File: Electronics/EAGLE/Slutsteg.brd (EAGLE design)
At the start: 100 x 160 mm, 151 parts, among them CN1 OSTYK33102030-2, CN2 OSTYK33102030-2, CN3 OSTYK33102030-2, CN4 OSTYK33102030-2, IC1 SPX1117M3-L-3-3_TR, IC10 LM324D, IC11 L78M12ABDT-TR, IC3 ESP32-WROVER-IE-4MB, IC4 TM8211, IC5 LM358LVIDR, IC6 TPA3244DDWR, IC7 TPA3251D2DDVR, IC8 LM324D, IC9 LM324D, J1 0532610671, SW1 PDB181-K420F-103A2, SW2 PDB181-K420F-103A2

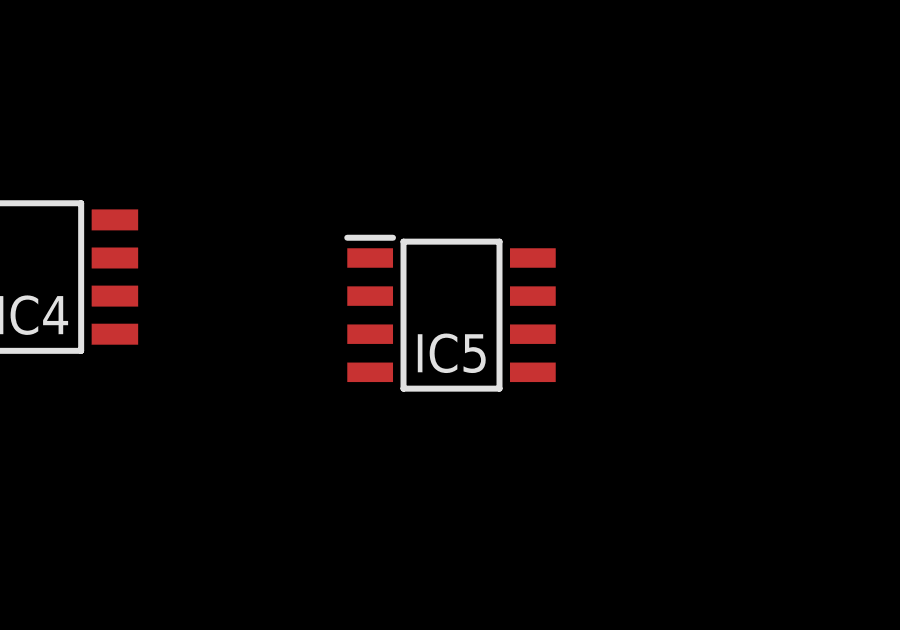
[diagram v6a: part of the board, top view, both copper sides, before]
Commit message: Changed OP-AMP for the DAC
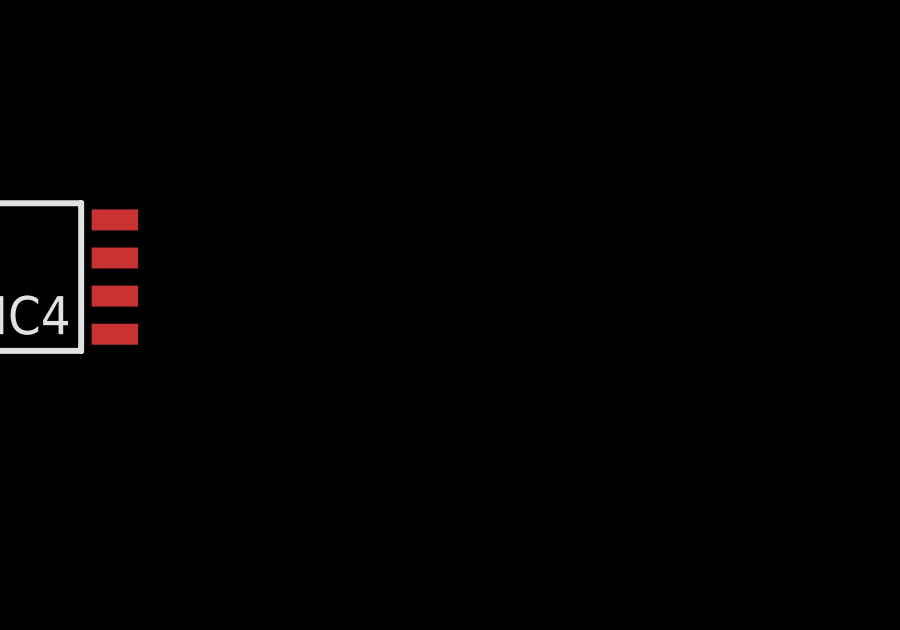
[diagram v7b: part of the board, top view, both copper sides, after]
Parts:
- removed IC5: LM358LVIDR, SamacSys_Parts:SOIC127P600X175-8N
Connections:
- net BLE-L: now also IC10.6, IC10.7; no longer IC5.6, IC5.7
- net BLE-R: now also IC10.1, IC10.2; no longer IC5.1, IC5.2
- net GND: now also IC10.11; no longer IC5.4
- net N$79: now also IC10.3; no longer IC5.3
- net N$81: now also IC10.5; no longer IC5.5
- net VDD: now also IC10.4; no longer IC5.8
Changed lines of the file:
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@@
 <attribute name="VALUE" x="-205.56" y="146.59" size="1.27" layer="27"/>
-</element>
-<element name="IC5" library="SamacSys_Parts" package="SOIC127P600X175-8N" override_package3d_urn="urn:adsk.eagle:package:27158186/2" override_package_urn="urn:adsk.eagle:footprint:27158187/1" override_locally_modified="yes" value="LM358LVIDR" x="-182.7" y="192.31" smashed="yes">
-<attribute name="ARROW_PART_NUMBER" value="LM358LVIDR" x="-182.7" y="192.31" size="1.778" layer="27" display="off"/>
-<attribute name="ARROW_PRICE-STOCK" value="https://www.arrow.com/en/products/lm358lvidr/texas-instruments" x="-182.7" y="192.31" size="1.778" layer="27" display="off"/>
-<attribute name="DESCRIPTION" value="2-Channel Industry-Standard Low-Voltage Operational Amplifier" x="-182.7" y="192.31" size="1.778" layer="27" display="off"/>
-<attribute name="HEIGHT" value="1.75mm" x="-182.7" y="192.31" size="1.778" layer="27" display="off"/>
-<attribute name="MANUFACTURER_NAME" value="Texas Instruments" x="-182.7" y="192.31" size="1.778" layer="27" display="off"/>
-<attribute name="MANUFACTURER_PART_NUMBER" value="LM358LVIDR" x="-182.7" y="192.31" size="1.778" layer="27" display="off"/>
-<attribute name="MOUSER_PART_NUMBER" value="595-LM358LVIDR" x="-182.7" y="192.31" size="1.778" layer="27" display="off"/>
-<attribute name="MOUSER_PRICE-STOCK" value="https://www.mouser.co.uk/ProductDetail/Texas-Instruments/LM358LVIDR/?qs=qSfuJ%252Bfl%2Fd53U%2FPkf9lZVw%3D%3D" x="-182.7" y="192.31" size="1.778" layer="27" display="off"/>
-<attribute name="NAME" x="-182.7" y="191.04" size="1.27" layer="25" align="center"/>
-<attribute name="VALUE" x="-182.7" y="194.85" size="1.27" layer="27" align="center"/>
 </element>
 <element name="R6" library="rcl" library_urn="urn:adsk.eagle:library:334" package="R0603" package3d_urn="urn:adsk.eagle:package:23555/3" value="10k/5%/0.1W" x="-206.83" y="136.43" smashed="yes">
@@
 <contactref element="C8" pad="2"/>
 <contactref element="C11" pad="2"/>
-<contactref element="IC5" pad="4"/>
 <contactref element="C13" pad="2"/>
 <contactref element="R7" pad="2"/>
-<contactref element="R10" pad="2"/>
 <contactref element="IC11" pad="4"/>
 <contactref element="C5" pad="2"/>
@@
 <contactref element="IC1" pad="1"/>
 <contactref element="C6" pad="2"/>
+<contactref element="R10" pad="2"/>
+<contactref element="IC10" pad="11"/>
 <wire x1="116.12" y1="129.87" x2="114.42" y2="134.95" width="0" layer="19" extent="1-1"/>
 <wire x1="114.42" y1="145.11" x2="114.42" y2="134.95" width="0" layer="19" extent="1-1"/>
@@
 <wire x1="-155.76" y1="225.86" x2="-157.46" y2="229.67" width="0" layer="19" extent="1-1"/>
 <wire x1="-161.518" y1="206.81" x2="-155.76" y2="225.86" width="0" layer="19" extent="1-1"/>
-<wire x1="-185.412" y1="190.405" x2="-161.518" y2="206.81" width="0" layer="19" extent="1-1"/>
-<wire x1="-199.42" y1="191.675" x2="-185.412" y2="190.405" width="0" layer="19" extent="1-1"/>
+<wire x1="-193.545" y1="237.764" x2="-157.46" y2="229.67" width="0" layer="19" extent="1-1"/>
+<wire x1="-199.42" y1="191.675" x2="-161.518" y2="206.81" width="0" layer="19" extent="1-1"/>
 <wire x1="-203.34" y1="189.77" x2="-199.42" y2="191.675" width="0" layer="19" extent="1-1"/>
 <wire x1="-203.34" y1="177.07" x2="-203.34" y2="189.77" width="0" layer="19" extent="1-1"/>
@@
 <wire x1="-205.98" y1="80.55" x2="-205.98" y2="105.95" width="0" layer="19" extent="1-1"/>
 <wire x1="-205.98" y1="75.47" x2="-205.98" y2="80.55" width="0" layer="19" extent="1-1"/>
-<wire x1="-193.545" y1="237.764" x2="-157.46" y2="229.67" width="0" layer="19" extent="1-1"/>
 <wire x1="-164.65" y1="124.26" x2="-205.98" y2="116.11" width="0" layer="19" extent="1-1"/>
 <wire x1="-164.65" y1="129.34" x2="-164.65" y2="124.26" width="0" layer="19" extent="1-1"/>
-<wire x1="-199.55" y1="-15" x2="-205.98" y2="75.47" width="0" layer="19" extent="1-1"/>
+<wire x1="-201.288" y1="-6" x2="-205.98" y2="75.47" width="0" layer="19" extent="1-1"/>
+<wire x1="-199.55" y1="-15" x2="-201.288" y2="-6" width="0" layer="19" extent="1-1"/>
 <wire x1="-208" y1="-20.7" x2="-199.55" y2="-15" width="0" layer="19" extent="1-1"/>
 <wire x1="-211.05" y1="-30" x2="-208" y2="-20.7" width="0" layer="19" extent="1-1"/>
@@
 <contactref element="C77" pad="1"/>
 <contactref element="C74" pad="1"/>
-<contactref element="IC5" pad="8"/>
 <contactref element="IC11" pad="3"/>
 <contactref element="D1" pad="1"/>
 <contactref element="IC1" pad="3"/>
 <contactref element="C4" pad="1"/>
+<contactref element="IC10" pad="4"/>
 <wire x1="-208" y1="-25.3" x2="-212.95" y2="-30" width="0" layer="19" extent="1-1"/>
 <wire x1="-206.35" y1="-17.28" x2="-208" y2="-25.3" width="0" layer="19" extent="1-1"/>
-<wire x1="-166.35" y1="124.26" x2="-206.35" y2="-17.28" width="0" layer="19" extent="1-1"/>
+<wire x1="-206.712" y1="-6" x2="-206.35" y2="-17.28" width="0" layer="19" extent="1-1"/>
+<wire x1="-166.35" y1="124.26" x2="-206.712" y2="-6" width="0" layer="19" extent="1-1"/>
 <wire x1="-166.35" y1="129.34" x2="-166.35" y2="124.26" width="0" layer="19" extent="1-1"/>
-<wire x1="-179.988" y1="194.215" x2="-166.35" y2="129.34" width="0" layer="19" extent="1-1"/>
-<wire x1="-166.942" y1="206.81" x2="-179.988" y2="194.215" width="0" layer="19" extent="1-1"/>
-<wire x1="-203.35" y1="199.93" x2="-179.988" y2="194.215" width="0" layer="19" extent="1-1"/>
+<wire x1="-166.942" y1="206.81" x2="-166.35" y2="129.34" width="0" layer="19" extent="1-1"/>
 <wire x1="-155.76" y1="233.48" x2="-166.942" y2="206.81" width="0" layer="19" extent="1-1"/>
 <wire x1="-155.76" y1="244.91" x2="-155.76" y2="233.48" width="0" layer="19" extent="1-1"/>
 <wire x1="-158.052" y1="261.42" x2="-155.76" y2="244.91" width="0" layer="19" extent="1-1"/>
 <wire x1="-137.98" y1="291.9" x2="-158.052" y2="261.42" width="0" layer="19" extent="1-1"/>
+<wire x1="-203.35" y1="199.93" x2="-166.942" y2="206.81" width="0" layer="19" extent="1-1"/>
 <wire x1="-16.55" y1="215.27" x2="-155.76" y2="233.48" width="0" layer="19" extent="1-1"/>
 <wire x1="-16.55" y1="210.19" x2="-16.55" y2="215.27" width="0" layer="19" extent="1-1"/>
@@
 </signal>
 <signal name="BLE-R">
-<contactref element="IC5" pad="1"/>
-<contactref element="IC5" pad="2"/>
 <contactref element="C9" pad="1"/>
-<wire x1="-185.412" y1="192.945" x2="-207.68" y2="126.27" width="0" layer="19" extent="1-1"/>
-<wire x1="-185.412" y1="194.215" x2="-185.412" y2="192.945" width="0" layer="19" extent="1-1"/>
-</signal>
-<signal name="BLE-L">
-<contactref element="IC5" pad="7"/>
-<contactref element="C14" pad="1"/>
-<contactref element="IC5" pad="6"/>
-<wire x1="-179.988" y1="191.675" x2="-207.68" y2="90.71" width="0" layer="19" extent="1-1"/>
-<wire x1="-179.988" y1="192.945" x2="-179.988" y2="191.675" width="0" layer="19" extent="1-1"/>
+<contactref element="IC10" pad="1"/>
+<contactref element="IC10" pad="2"/>
+<wire x1="-206.712" y1="-2.19" x2="-206.712" y2="-3.46" width="0" layer="19" extent="1-1"/>
+<wire x1="-207.68" y1="126.27" x2="-206.712" y2="-2.19" width="0" layer="19" extent="1-1"/>
 </signal>
 <signal name="N$46">
@@
 <signal name="N$79">
 <contactref element="R8" pad="1"/>
-<contactref element="IC5" pad="3"/>
 <contactref element="C10" pad="1"/>
+<contactref element="IC10" pad="3"/>
+<wire x1="-207.68" y1="121.19" x2="-206.712" y2="-4.73" width="0" layer="19" extent="1-1"/>
 <wire x1="-207.68" y1="131.35" x2="-207.68" y2="121.19" width="0" layer="19" extent="1-1"/>
-<wire x1="-185.412" y1="191.675" x2="-207.68" y2="131.35" width="0" layer="19" extent="1-1"/>
 </signal>
 <signal name="N$80">
@@
 </signal>
 <signal name="N$81">
-<contactref element="IC5" pad="5"/>
+<contactref element="R9" pad="2"/>
+<contactref element="IC10" pad="5"/>
 <contactref element="C12" pad="1"/>
-<contactref element="R9" pad="2"/>
+<wire x1="-205.98" y1="100.87" x2="-206.712" y2="-7.27" width="0" layer="19" extent="1-1"/>
 <wire x1="-207.68" y1="111.03" x2="-205.98" y2="100.87" width="0" layer="19" extent="1-1"/>
-<wire x1="-179.988" y1="190.405" x2="-207.68" y2="111.03" width="0" layer="19" extent="1-1"/>
 </signal>
 <signal name="N$82">
@@
 </signal>
 <signal name="N$83">
-<contactref element="C14" pad="2"/>
 <contactref element="R9" pad="1"/>
 <contactref element="R11" pad="2"/>
+<contactref element="C14" pad="2"/>
 <contactref element="R10" pad="1"/>
 <wire x1="-205.98" y1="90.71" x2="-207.68" y2="75.47" width="0" layer="19" extent="1-1"/>
@@
 <contactref element="C22" pad="1"/>
 </signal>
+<signal name="BLE-L">
+<contactref element="IC10" pad="7"/>
+<contactref element="IC10" pad="6"/>
+<contactref element="C14" pad="1"/>
+<wire x1="-206.712" y1="-8.54" x2="-206.712" y2="-9.81" width="0" layer="19" extent="1-1"/>
+<wire x1="-207.68" y1="90.71" x2="-206.712" y2="-8.54" width="0" layer="19" extent="1-1"/>
+</signal>
 </signals>

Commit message: Changed footprints for caps
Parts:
- removed C76: 1uF/25V, rcl:C0603
- added C25: 1uF/50V, rcl:C0805
- C78, C79: value 1uF/25V -> 1uF/50V; device rcl:C0603 -> rcl:C0805
- moved C79 334.9 mm to (-212.0, -93.0)
- moved C78 331.8 mm to (-212.0, -86.0)
- moved J1 303.9 mm to (95.2, 152.3), turned to 90 degrees
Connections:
- net GND: now also C79.2; no longer C76.2
- net N$46: now also C25.1; no longer C78.2
- net N$47: now also C78.1; no longer C79.2
- net N$50: now also C79.1; no longer C76.1
- net SIG_IN_LEFT: now also C25.2; no longer C78.1
- net SIG_IN_RIGHT: now also C78.2; no longer C79.1
